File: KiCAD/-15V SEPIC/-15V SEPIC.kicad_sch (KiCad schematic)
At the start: 17 parts, among them U1 LT3579

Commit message: work on speic schematic and PCB
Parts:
- D2: footprint (none) -> footprints:DO-221AC
- R1, R2, R3, R4: footprint Resistor_SMD:R_01005_0402Metric -> Resistor_SMD:R_0402_1005Metric
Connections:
- net GND: now also D2.1 (K); no longer D2.2 (A)
- net at C10.2, L1.4: now also D2.2 (A); no longer D2.1 (K)
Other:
- moved on the sheet: D2
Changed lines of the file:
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@@
   (junction (at 201.93 118.11) (diameter 0) (color 0 0 0 0)
   )
+  (junction (at 195.58 78.74) (diameter 0) (color 0 0 0 0)
+  )
   (junction (at 129.54 73.66) (diameter 0) (color 0 0 0 0)
   )
+  (junction (at 170.18 73.66) (diameter 0) (color 0 0 0 0)
+  )
   (junction (at 116.84 118.11) (diameter 0) (color 0 0 0 0)
   )
@@
   (junction (at 149.86 73.66) (diameter 0) (color 0 0 0 0)
   )
-  (junction (at 170.18 73.66) (diameter 0) (color 0 0 0 0)
-  )
   (junction (at 152.4 73.66) (diameter 0) (color 0 0 0 0)
   )
@@
   )
   (junction (at 179.07 118.11) (diameter 0) (color 0 0 0 0)
-  )
-  (junction (at 195.58 78.74) (diameter 0) (color 0 0 0 0)
   )
   (junction (at 138.43 118.11) (diameter 0) (color 0 0 0 0)
@@
     (stroke (width 0) (type default))
   )
+  (wire (pts (xy 189.23 78.74) (xy 195.58 78.74))
+    (stroke (width 0) (type default))
+  )
   (wire (pts (xy 144.78 73.66) (xy 147.32 73.66))
     (stroke (width 0) (type default))
@@
   )
   (wire (pts (xy 109.22 99.06) (xy 107.95 99.06))
-    (stroke (width 0) (type default))
-  )
-  (wire (pts (xy 189.23 78.74) (xy 195.58 78.74))
     (stroke (width 0) (type default))
   )
@@
       (effects (font (size 1.27 1.27)) (justify left))
     )
-    (property "Footprint" "Resistor_SMD:R_01005_0402Metric" (at 115.062 111.76 90)
+    (property "Footprint" "Resistor_SMD:R_0402_1005Metric" (at 115.062 111.76 90)
       (effects (font (size 1.27 1.27)) hide)
     )
@@
       (effects (font (size 1.27 1.27)))
     )
-    (property "Footprint" "Resistor_SMD:R_01005_0402Metric" (at 167.64 100.838 90)
+    (property "Footprint" "Resistor_SMD:R_0402_1005Metric" (at 167.64 100.838 90)
       (effects (font (size 1.27 1.27)) hide)
     )
@@
     )
   )
-  (symbol (lib_id "Device:D_Schottky") (at 170.18 77.47 270) (unit 1)
-    (in_bom yes) (on_board yes) (dnp no)
-    (property "Reference" "D2" (at 172.72 76.5175 90)
-      (effects (font (size 1.27 1.27)) (justify left))
-    )
-    (property "Value" "VSSAF5L45" (at 171.45 81.28 90)
-      (effects (font (size 1.27 1.27)) (justify left))
-    )
-    (property "Footprint" "" (at 170.18 77.47 0)
+  (symbol (lib_id "Device:D_Schottky") (at 170.18 77.47 90) (unit 1)
+    (in_bom yes) (on_board yes) (dnp no)
+    (property "Reference" "D2" (at 175.26 78.74 90)
+      (effects (font (size 1.27 1.27)) (justify left))
+    )
+    (property "Value" "VSSAF5L45" (at 181.61 73.66 90)
+      (effects (font (size 1.27 1.27)) (justify left))
+    )
+    (property "Footprint" "footprints:DO-221AC" (at 170.18 77.47 0)
       (effects (font (size 1.27 1.27)) hide)
     )
@@
       (effects (font (size 1.27 1.27)))
     )
-    (property "Footprint" "Resistor_SMD:R_01005_0402Metric" (at 113.03 100.838 90)
+    (property "Footprint" "Resistor_SMD:R_0402_1005Metric" (at 113.03 100.838 90)
       (effects (font (size 1.27 1.27)) hide)
     )
@@
       (effects (font (size 1.27 1.27)))
     )
-    (property "Footprint" "Resistor_SMD:R_01005_0402Metric" (at 165.1 90.678 90)
-      (effects (font (size 1.27 1.27)) hide)
-    )
+    (property "Footprint" "Resistor_SMD:R_0402_1005Metric" (at 165.1 90.678 90)
+      (effects (font (size 1.27 1.27)) hide)
+    )

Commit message: update PCB
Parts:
- added C11: 100n, Capacitor_SMD:C_0402_1005Metric, symbol Device:C
- added J1: Conn_01x04_Pin, Connector_PinHeader_2.54mm:PinHeader_1x04_P2.54mm_Horizontal, symbol Connector:Conn_01x04_Pin
- added TP3, TP5: TestPoint, TestPoint:TestPoint_Pad_D1.0mm, symbol Connector:TestPoint
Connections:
- net -15V: now also J1.3 (Pin_3)
- net GND: now also C11.2, J1.2 (Pin_2), J1.4 (Pin_4), TP5.1
- net Vin (12V - 15V): now also C11.1, J1.1 (Pin_1)
- net at C10.1, L1.3, U1.10 (SW1)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: now also TP3.1
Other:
- note added: "buffer cap for Vin LT3579"

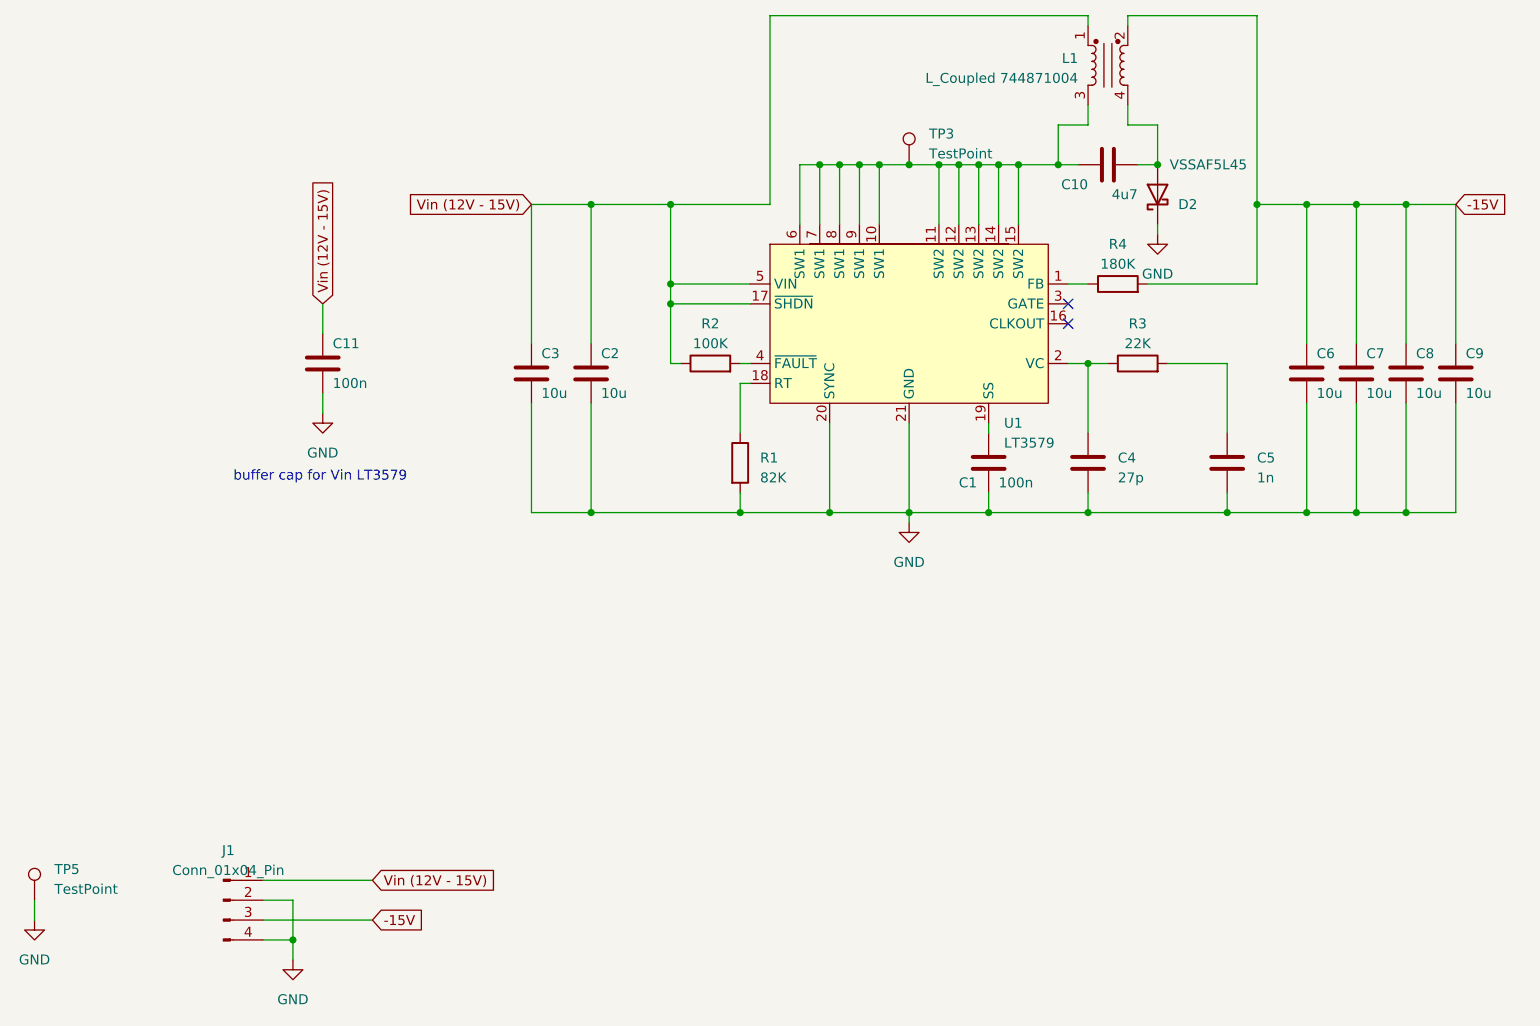
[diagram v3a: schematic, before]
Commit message: Added SEPIC symbol and footprint and worked on main board
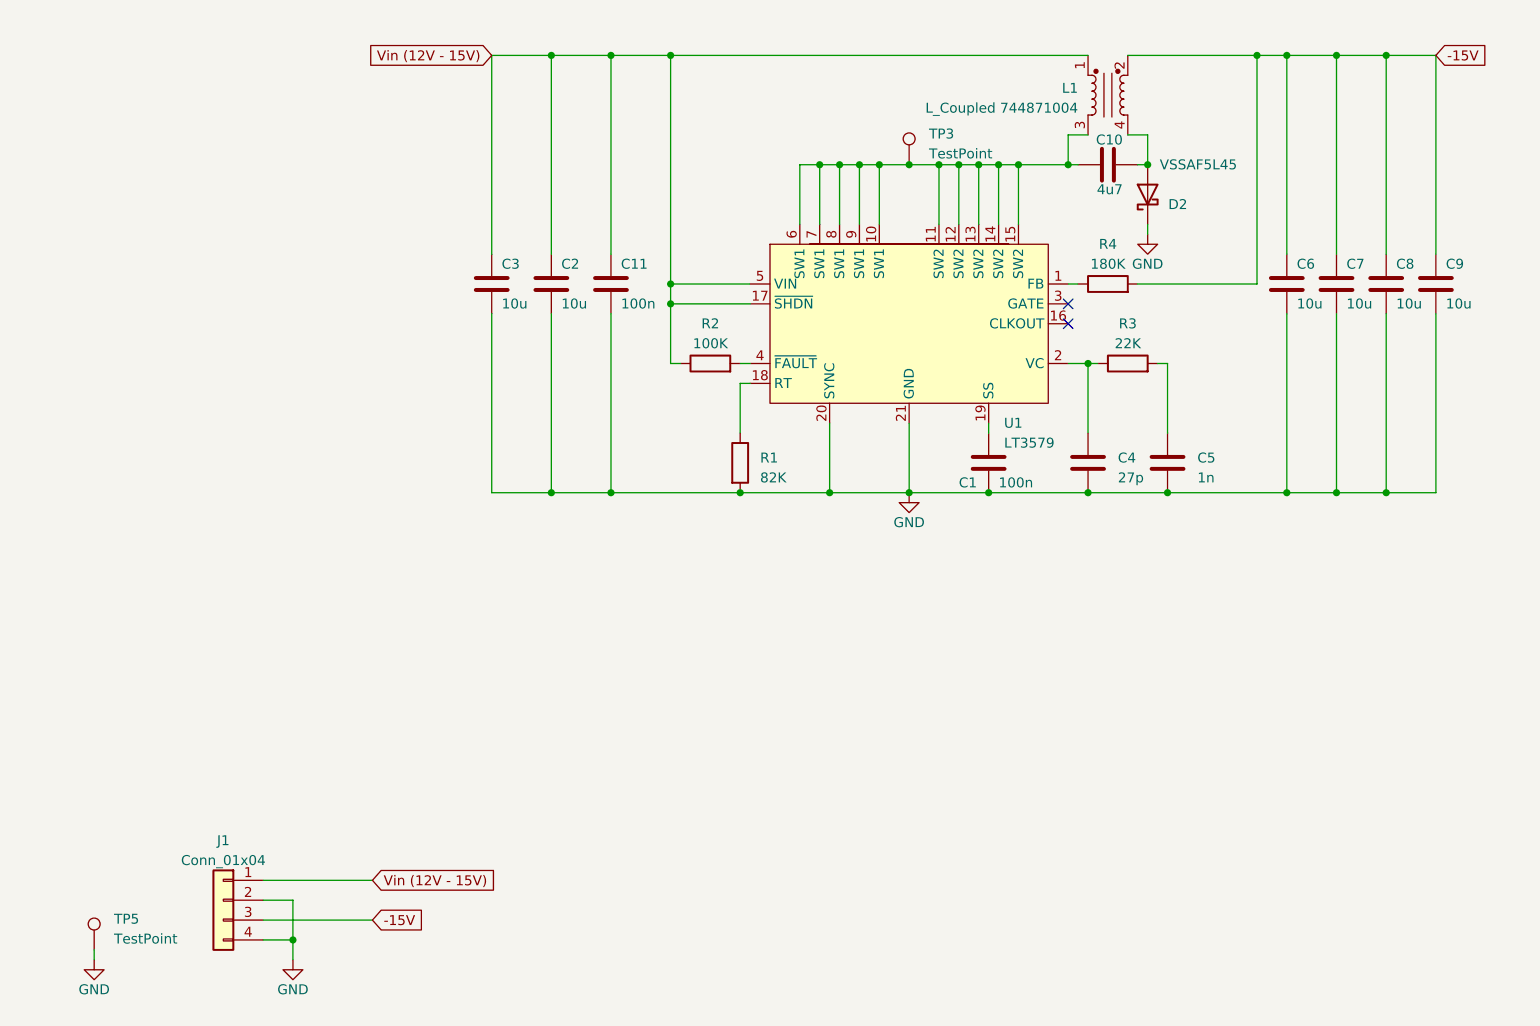
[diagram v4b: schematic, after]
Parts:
- removed J1: Conn_01x04_Pin, Connector_PinHeader_2.54mm:PinHeader_1x04_P2.54mm_Horizontal, symbol Connector:Conn_01x04_Pin
- added J1: Conn_01x04, Connector_PinHeader_2.54mm:PinHeader_1x04_P2.54mm_Horizontal, symbol Connector_Generic:Conn_01x04
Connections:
- net -15V: now also J1.3 (Pin_3)
- net GND: now also J1.2 (Pin_2), J1.4 (Pin_4)
- net Vin (12V - 15V): now also J1.1 (Pin_1)
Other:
- note removed: "buffer cap for Vin LT3579"
- moved on the sheet: C11, C2, C3, C5, C6, C7, C8, C9, D2, L1, R3, R4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
